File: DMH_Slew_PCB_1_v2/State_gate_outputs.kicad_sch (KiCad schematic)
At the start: 24 parts, among them J4 TS_Jack_6.35mm_Sw, J5 TS_Jack_6.35mm_Sw, Q5 BC548, Q6 BC548, U1 TL074

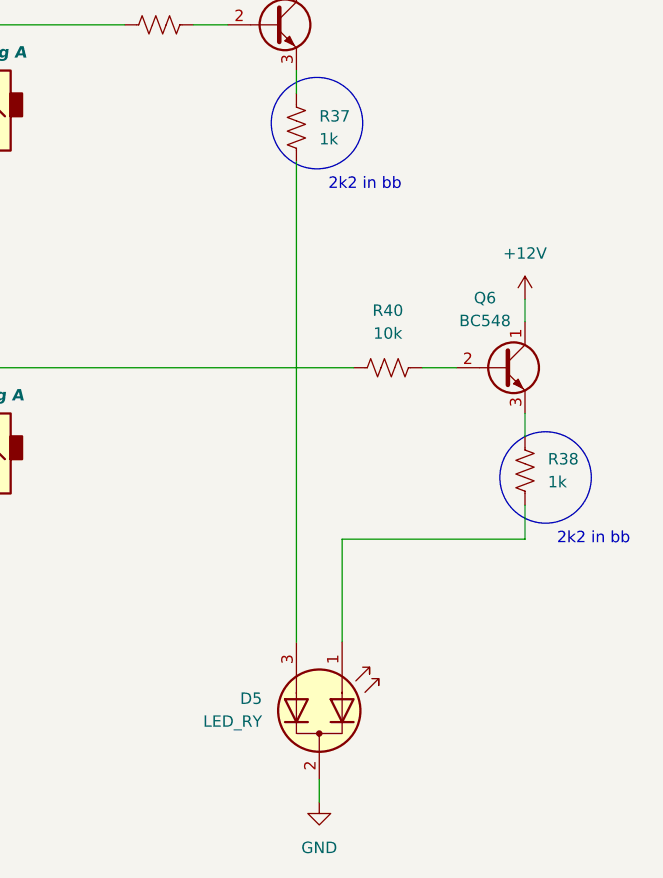
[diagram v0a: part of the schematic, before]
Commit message: Redesigned front panel in v2
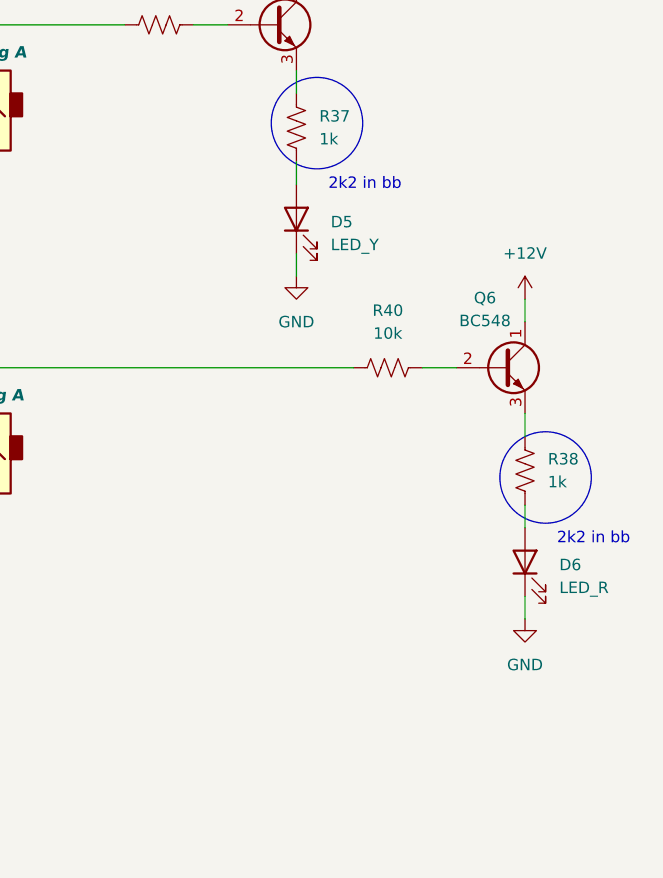
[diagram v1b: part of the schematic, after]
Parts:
- removed D5: LED_RY, SynthStuff:LED_D3.0mm-2color, symbol Device:LED_Dual_AKA
- added D5: LED_Y, LED_THT:LED_D3.0mm, symbol Device:LED
- added D6: LED_R, LED_THT:LED_D3.0mm, symbol Device:LED
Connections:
- net GND: now also D5.1 (K), D6.1 (K)
- net at R38.2: now also D6.2 (A)
- net at R37.2: now also D5.2 (A)

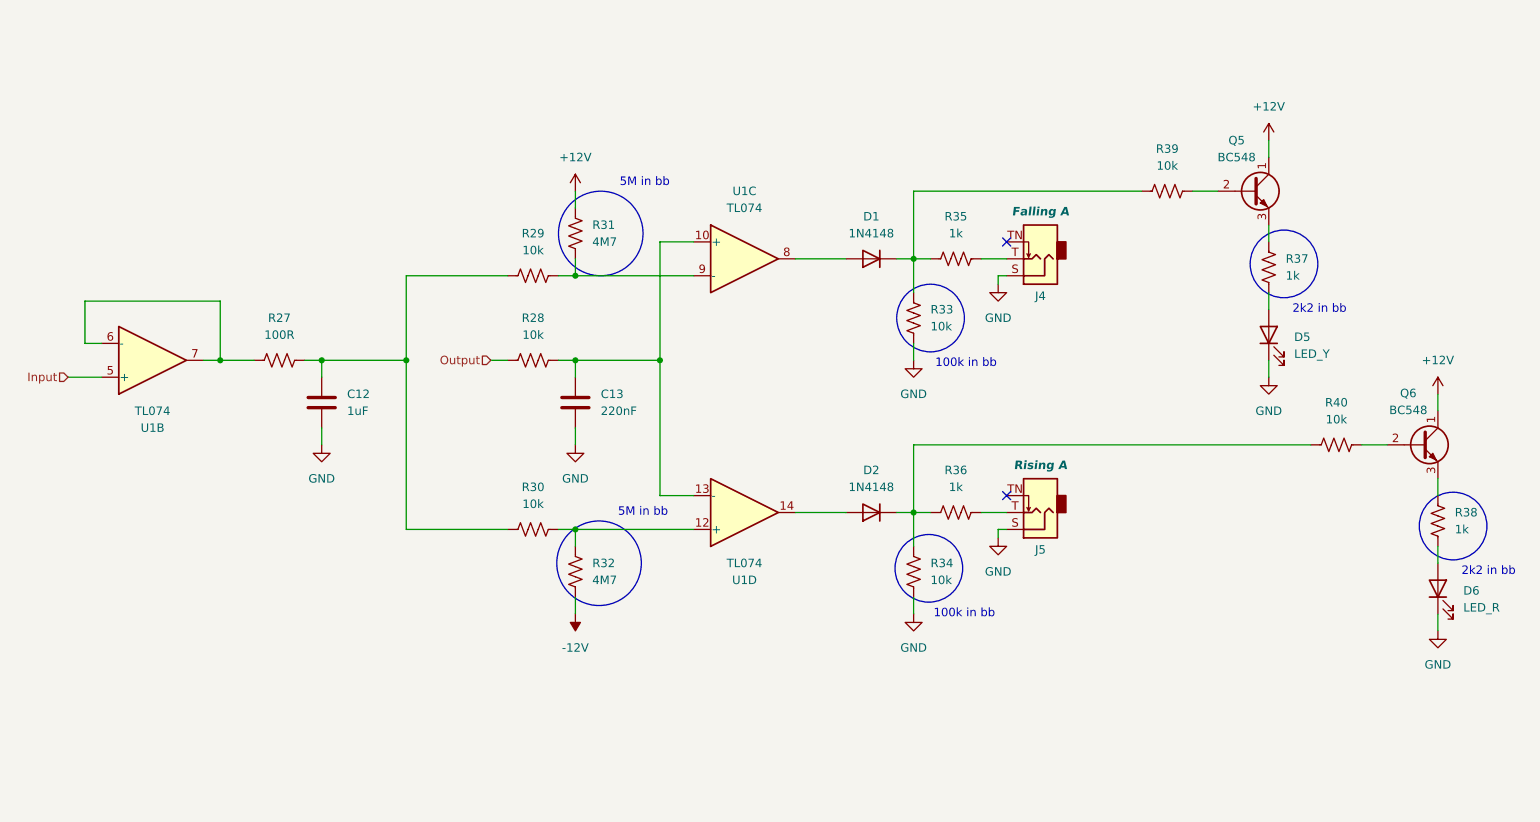
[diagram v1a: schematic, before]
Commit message: Breadboard tests done
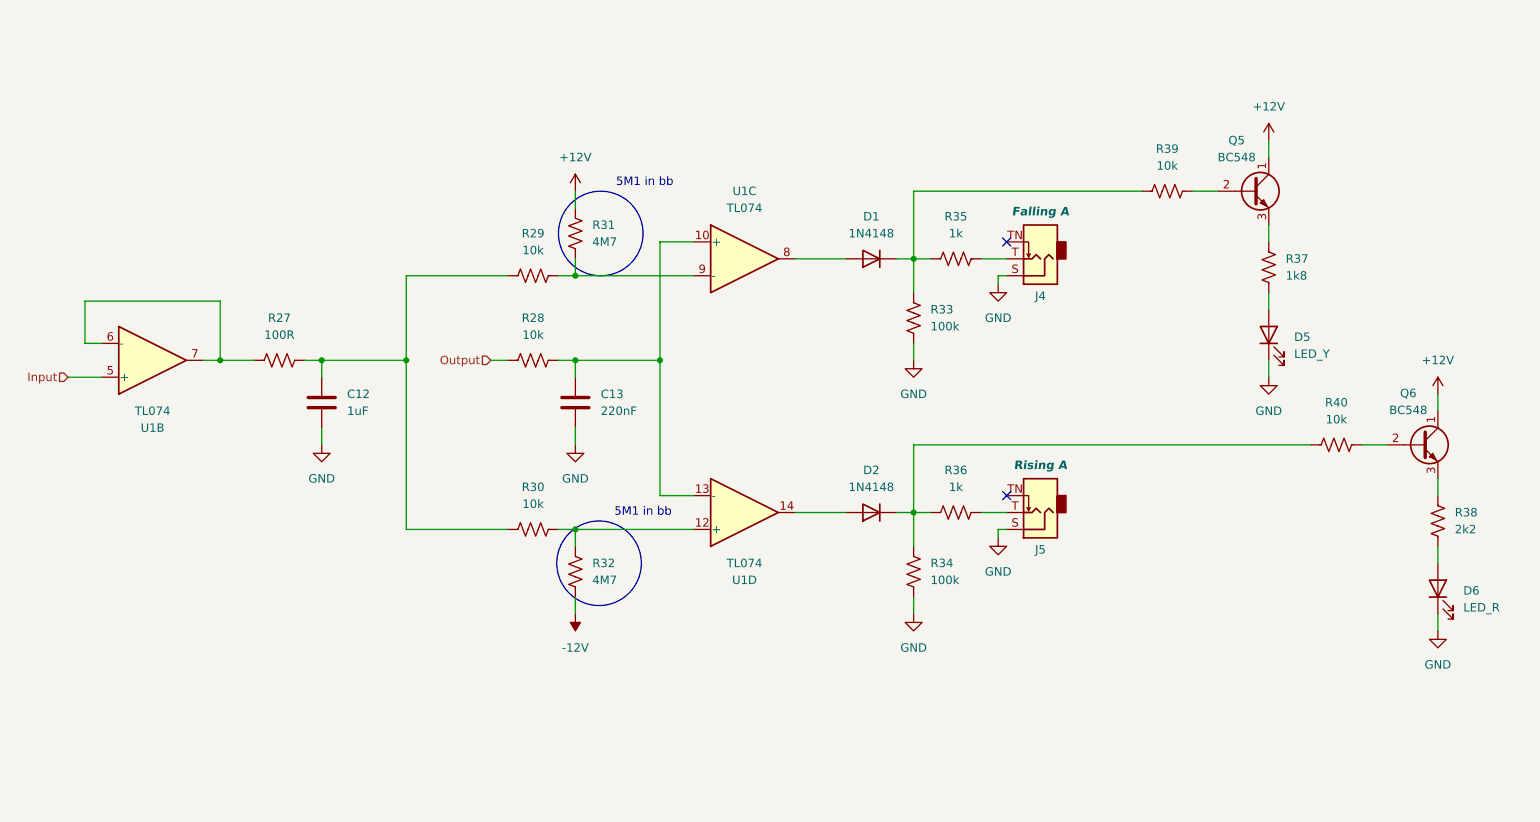
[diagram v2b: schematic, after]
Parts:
- R33, R34: value 10k -> 100k
- R37: value 1k -> 1k8
- R38: value 1k -> 2k2
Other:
- note added: "5M1 in bb"
- note removed: "100k in bb"
- note removed: "2k2 in bb"
- note removed: "5M in bb"
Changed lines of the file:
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@@
-	)
-	(circle
-		(center 180.086 107.442)
-		(radius 5.08)
-		(stroke
-			(width 0)
-			(type default)
-		)
-		(fill
-			(type none)
-		)
-	)
-	(circle
-		(center 258.826 101.092)
-		(radius 5.08)
-		(stroke
-			(width 0)
-			(type default)
-		)
-		(fill
-			(type none)
-		)
 	)
 	(circle
@@
 	)
 	(circle
-		(center 180.34 69.85)
-		(radius 5.08)
+		(center 130.556 106.68)
+		(radius 6.35)
 		(stroke
 			(width 0)
@@
 		)
 	)
-	(circle
-		(center 233.426 61.722)
-		(radius 5.08)
-		(stroke
-			(width 0)
-			(type default)
-		)
-		(fill
-			(type none)
-		)
-	)
-	(circle
-		(center 130.556 106.68)
-		(radius 6.35)
-		(stroke
-			(width 0)
-			(type default)
-		)
-		(fill
-			(type none)
-		)
-	)
-	(text "2k2 in bb"
-		(exclude_from_sim no)
-		(at 238.76 68.58 0)
-		(effects
-			(font
-				(size 1.27 1.27)
-			)
-		)
-	)
-	(text "100k in bb"
-		(exclude_from_sim no)
-		(at 185.674 76.708 0)
-		(effects
-			(font
-				(size 1.27 1.27)
-			)
-		)
-	)
-	(text "100k in bb"
-		(exclude_from_sim no)
-		(at 185.42 114.3 0)
-		(effects
-			(font
-				(size 1.27 1.27)
-			)
-		)
-	)
-	(text "5M in bb"
+	(text "5M1 in bb"
 		(exclude_from_sim no)
 		(at 137.16 99.06 0)
@@
 		)
 	)
-	(text "5M in bb"
+	(text "5M1 in bb"
 		(exclude_from_sim no)
 		(at 137.414 49.53 0)
-		(effects
-			(font
-				(size 1.27 1.27)
-			)
-		)
-	)
-	(text "2k2 in bb"
-		(exclude_from_sim no)
-		(at 264.16 107.95 0)
 		(effects
 			(font
@@
 			)
 		)
-		(property "Value" "10k"
+		(property "Value" "100k"
 			(at 180.34 109.2199 0)
 			(effects
@@
 			)
 		)
-		(property "Value" "10k"
+		(property "Value" "100k"
 			(at 180.34 71.1199 0)
 			(effects
@@
 			)
 		)
-		(property "Value" "1k"
+		(property "Value" "2k2"
 			(at 259.08 101.5999 0)
 			(effects
@@
 			)
 		)
-		(property "Value" "1k"
+		(property "Value" "1k8"
 			(at 233.68 63.4999 0)
 			(effects

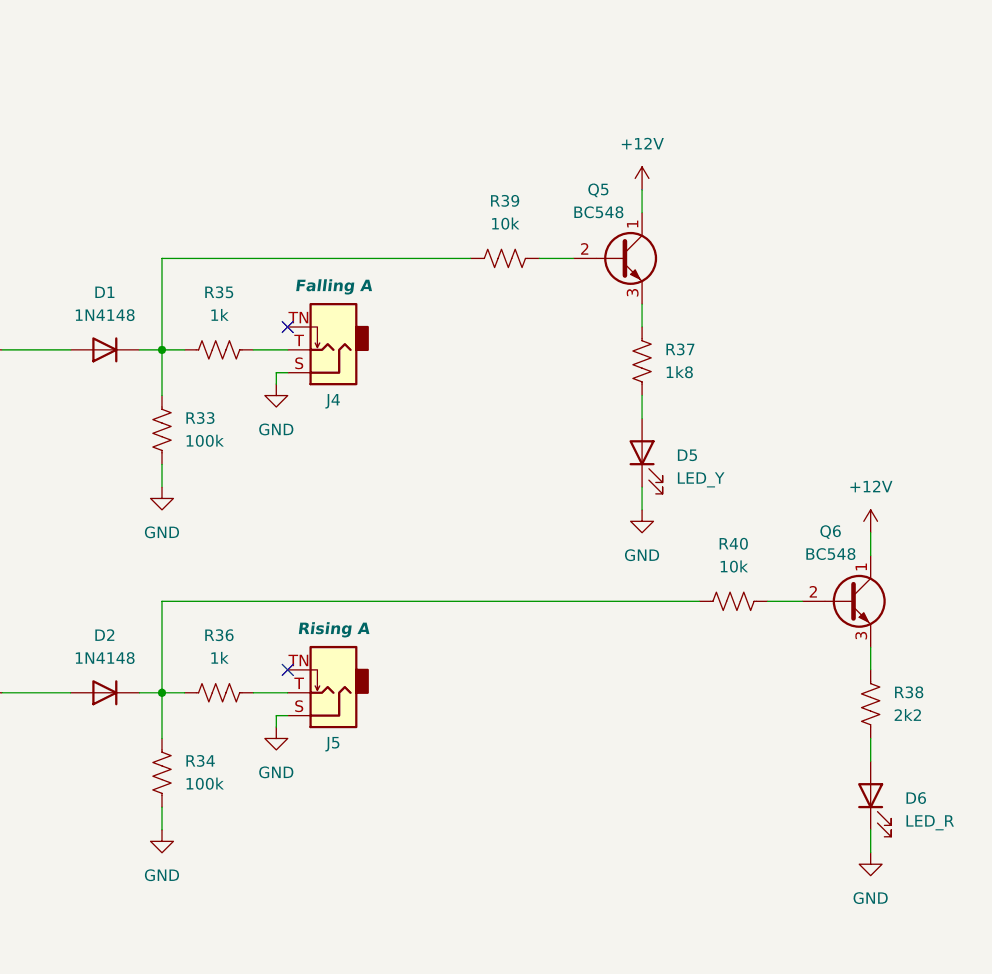
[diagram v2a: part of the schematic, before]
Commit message: Separating PCB 1 and 2 in schematic
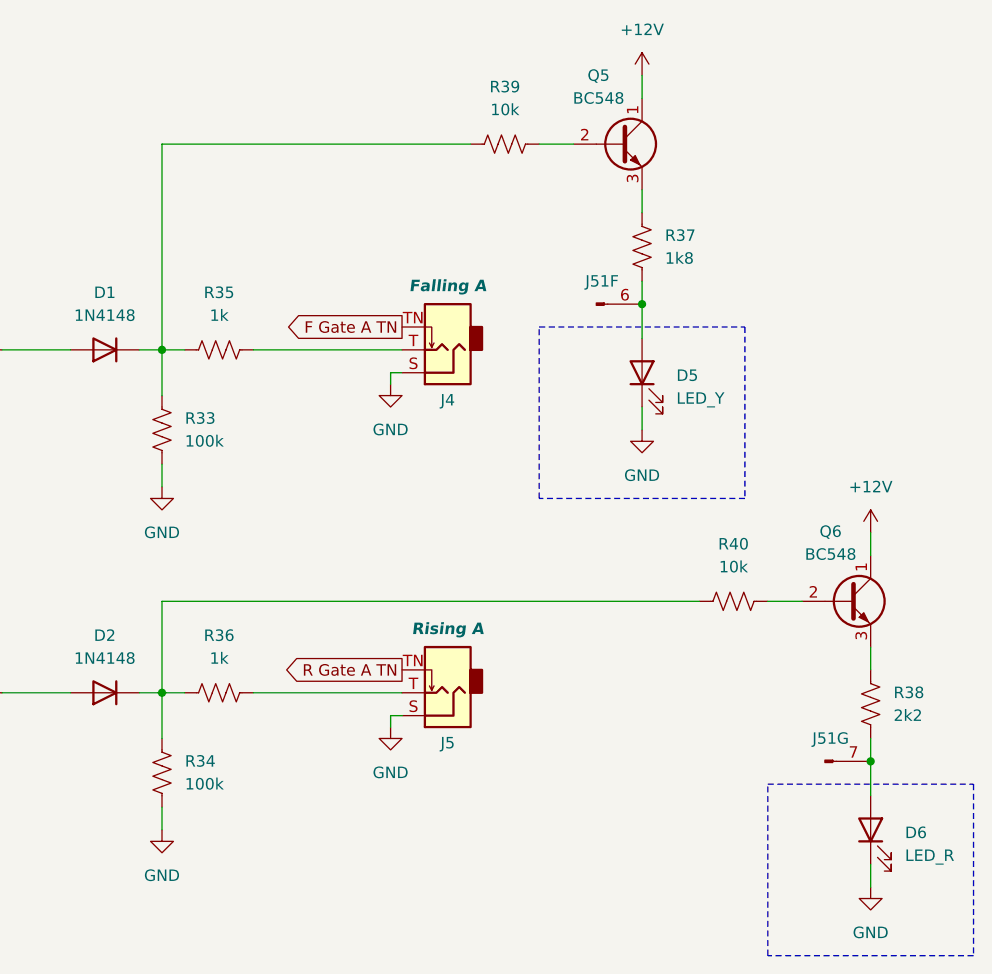
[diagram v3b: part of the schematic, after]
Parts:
- added J51: Conn_01x08_PinHeader, Connector_PinHeader_2.54mm:PinHeader_1x08_P2.54mm_Vertical, symbol SynthStuff:Conn_01x08_PinHeader
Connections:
- net F Gate A TN: now reaches J4.TN
- net R Gate A TN: now reaches J5.TN
- net at D6.2 (A), R38.2: now also J51.7 (Pin_7)
- net at D5.2 (A), R37.2: now also J51.6 (Pin_6)
- no-connect marks 2 -> 0
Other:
- moved on the sheet: D5, D6, J4, J5, Q5, R37, R39
